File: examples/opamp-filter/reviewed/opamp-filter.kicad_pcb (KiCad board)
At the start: 2 copper layers, 58 x 42 mm, 22 parts, among them J1 IN, J2 5V, J3 OUT, U1 MCP6001R, U2 MCP6001R

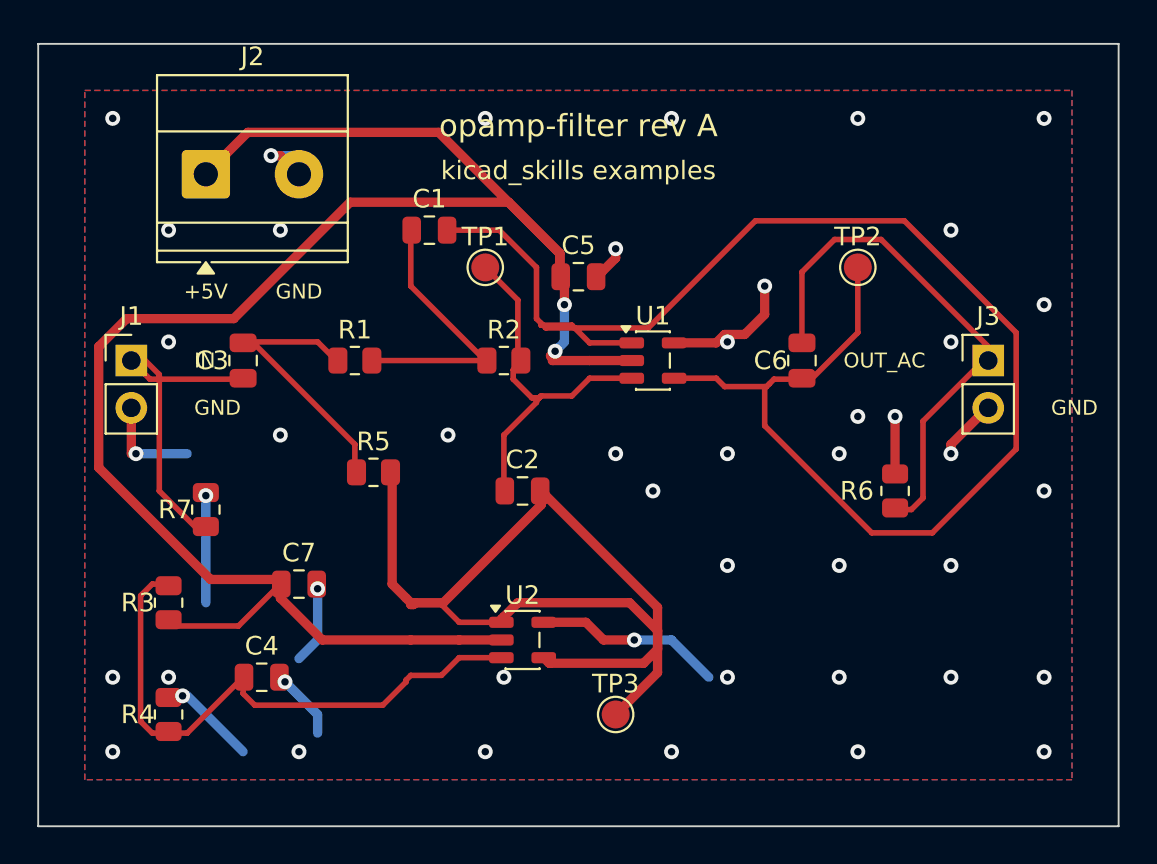
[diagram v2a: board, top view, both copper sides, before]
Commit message: Rip up copper that tours, and put a footprint's zones where the footprint is
The plots showed three things on the artwork side that no rule reported.

**A track that goes round the board to cover thirteen millimetres.** The
op-amp's feedback wrap had to get from one side of a SOT-23-5 to the other
and, routed last, took fifty-six millimetres of tour because everything
nearer was already spoken for. That is an ordering problem, so the loop that
fixes ordering fixes it: `_route_all` now reports what each track cost
against `route.wander`'s own baseline - imported, not copied, so the two
cannot drift - and the worst tour goes to the front and the set is routed
again. A track that still tours from first pick has nowhere better to be and
is left alone. The default order is shortest-first for the same reason: a
thirteen millimetre connection has few ways to be made and a forty
millimetre one has many. The learned order is now written on every change,
not only on success, because an afternoon of rip-ups is worth keeping when
the machine goes away in the middle.

**A keep-out sitting at the origin.** A footprint may carry zones of its own
and KiCad stores *those* in board coordinates while everything else in a
footprint is stored relative to it. The Pico module's two pad keep-outs had
been at (0, -6) for four rounds - off the board, keeping nothing out. DRC is
silent because an empty region violates no rule, and the only visible sign
was the plot: "fit to page" fits the bounding box, so every view of that
board came out at half scale in one corner with the rest blank.
`layout.zone_outside_outline` reports it; the placer moves it.

**Silkscreen printed through silkscreen.** The schematic has
`readability.text_over_text` and the board had nothing, though the board is
the harder case - a sheet can be zoomed and a bare board cannot.
`silk.text_over_text` measures it from the font size the file states; on
KiCad's demo boards it fires on 6 of 16, 173 times. The generator places t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
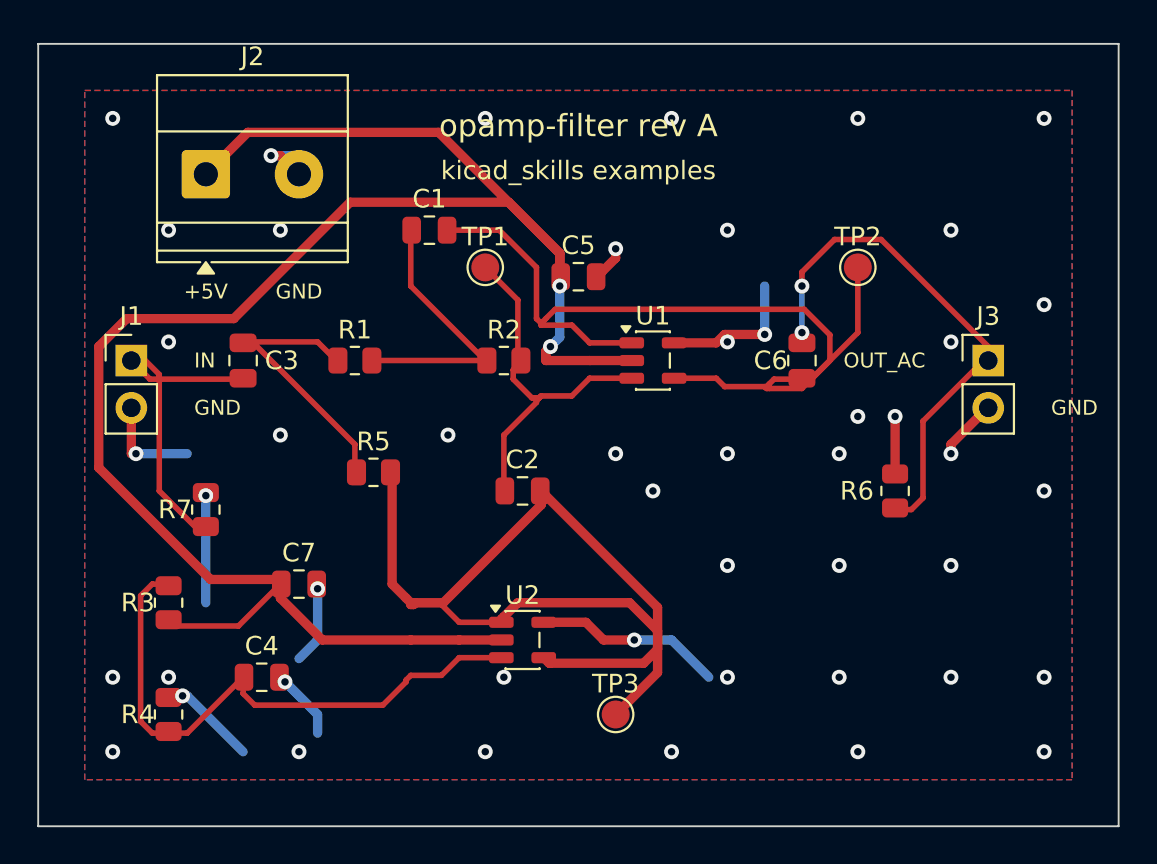
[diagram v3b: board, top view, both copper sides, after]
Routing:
- net /OUT: track 85.4 -> 50.9 mm
- net GND: track 53.8 -> 54.5 mm, vias 47 -> 48
- net /OUT_AC: vias 0 -> 2
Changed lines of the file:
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@@
     (tags "capacitor")
     (property "Reference" "C3"
-      (at 0.0 -1.68 0)
+      (at 0.0 2.075 0)
       (layer "F.SilkS")
       (effects
@@
     )
     (property "Voltage" "25V"
-      (at 0.0 -1.68 0)
+      (at 0.0 2.075 0)
       (layer "F.Fab")
       (hide yes)
@@
     )
     (property "Tolerance" "10%"
-      (at 0.0 -1.68 0)
+      (at 0.0 2.075 0)
       (layer "F.Fab")
       (hide yes)
@@
     )
     (property "MPN" "CL21B105KBFNNNE"
-      (at 0.0 -1.68 0)
+      (at 0.0 2.075 0)
       (layer "F.Fab")
       (hide yes)
@@
     )
     (property "Manufacturer" "Samsung"
-      (at 0.0 -1.68 0)
+      (at 0.0 2.075 0)
       (layer "F.Fab")
       (hide yes)
@@
     )
     (property "Datasheet" "https://product.samsungsem.com/mlcc/CL21B105KBFNNNE.do"
-      (at 0.0 -1.68 0)
+      (at 0.0 2.075 0)
       (layer "F.Fab")
       (hide yes)
@@
 	(segment (start 128.65 75.1) (end 127.0 75.1) (width 0.3) (layer "F.Cu") (net 7))
 	(segment (start 131.8625 77.0) (end 129.6 77.0) (width 0.5) (layer "F.Cu") (net 2))
-	(segment (start 129.6 77.0) (end 127.604 77.0) (width 0.5) (layer "F.Cu") (net 2))
-	(segment (start 127.604 77.0) (end 127.604 76.854) (width 0.5) (layer "F.Cu") (net 2))
-	(segment (start 127.604 76.854) (end 127.5 76.75) (width 0.5) (layer "F.Cu") (net 2))
-	(segment (start 127.5 76.75) (end 127.75 76.5) (width 0.5) (layer "F.Cu") (net 2))
+	(segment (start 129.6 77.0) (end 127.25 77.0) (width 0.5) (layer "F.Cu") (net 2))
+	(segment (start 127.25 77.0) (end 127.25 76.75) (width 0.5) (layer "F.Cu") (net 2))
+	(segment (start 127.25 76.75) (end 127.25 76.5) (width 0.5) (layer "F.Cu") (net 2))
+	(segment (start 127.25 76.5) (end 127.5 76.25) (width 0.5) (layer "F.Cu") (net 2))
 	(segment (start 131.8625 77.95) (end 129.6 77.95) (width 0.3) (layer "F.Cu") (net 3))
 	(segment (start 129.6 77.95) (end 128.65 78.9) (width 0.3) (layer "F.Cu") (net 3))
@@
 	(segment (start 134.1375 76.05) (end 136.4 76.05) (width 0.5) (layer "F.Cu") (net 1))
 	(segment (start 136.4 76.05) (end 136.85 75.6) (width 0.5) (layer "F.Cu") (net 1))
-	(segment (start 136.85 75.6) (end 137.925 75.6) (width 0.5) (layer "F.Cu") (net 1))
-	(segment (start 137.925 75.6) (end 139.0 74.525) (width 0.5) (layer "F.Cu") (net 1))
-	(segment (start 139.0 74.525) (end 139.0 73.0) (width 0.5) (layer "F.Cu") (net 1))
+	(segment (start 136.85 75.6) (end 139.0 75.6) (width 0.5) (layer "F.Cu") (net 1))
 	(segment (start 134.1375 77.95) (end 136.4 77.95) (width 0.3) (layer "F.Cu") (net 7))
 	(segment (start 136.4 77.95) (end 136.85 78.4) (width 0.3) (layer "F.Cu") (net 7))
@@
 	(segment (start 126.75 79.25) (end 126.75 79.15) (width 0.3) (layer "F.Cu") (net 3))
 	(segment (start 126.75 79.15) (end 127.0 78.9) (width 0.3) (layer "F.Cu") (net 3))
-	(segment (start 127.0 75.1) (end 127.1 75.1) (width 0.3) (layer "F.Cu") (net 7))
-	(segment (start 127.1 75.1) (end 127.25 75.25) (width 0.3) (layer "F.Cu") (net 7))
-	(segment (start 127.25 75.25) (end 132.75 75.25) (width 0.3) (layer "F.Cu") (net 7))
-	(segment (start 132.75 75.25) (end 138.5 69.5) (width 0.3) (layer "F.Cu") (net 7))
-	(segment (start 138.5 69.5) (end 146.5 69.5) (width 0.3) (layer "F.Cu") (net 7))
-	(segment (start 146.5 69.5) (end 152.5 75.5) (width 0.3) (layer "F.Cu") (net 7))
-	(segment (start 152.5 75.5) (end 152.5 81.75) (width 0.3) (layer "F.Cu") (net 7))
-	(segment (start 152.5 81.75) (end 148.0 86.25) (width 0.3) (layer "F.Cu") (net 7))
-	(segment (start 148.0 86.25) (end 144.75 86.25) (width 0.3) (layer "F.Cu") (net 7))
-	(segment (start 144.75 86.25) (end 139.0 80.5) (width 0.3) (layer "F.Cu") (net 7))
-	(segment (start 139.0 80.5) (end 139.0 78.4) (width 0.3) (layer "F.Cu") (net 7))
+	(segment (start 127.0 75.1) (end 127.0 75.0) (width 0.3) (layer "F.Cu") (net 7))
+	(segment (start 127.0 75.0) (end 127.25 74.75) (width 0.3) (layer "F.Cu") (net 7))
+	(segment (start 127.25 74.75) (end 127.75 74.25) (width 0.3) (layer "F.Cu") (net 7))
+	(segment (start 127.75 74.25) (end 141.125 74.25) (width 0.3) (layer "F.Cu") (net 7))
+	(segment (start 141.125 74.25) (end 142.5 75.625) (width 0.3) (layer "F.Cu") (net 7))
+	(segment (start 142.5 75.625) (end 142.5 77.0) (width 0.3) (layer "F.Cu") (net 7))
+	(segment (start 142.5 77.0) (end 141.0 78.5) (width 0.3) (layer "F.Cu") (net 7))
+	(segment (start 141.0 78.5) (end 139.25 78.5) (width 0.3) (layer "F.Cu") (net 7))
+	(segment (start 139.25 78.5) (end 139.1 78.5) (width 0.3) (layer "F.Cu") (net 7))
+	(segment (start 139.1 78.5) (end 139.0 78.4) (width 0.3) (layer "F.Cu") (net 7))
 	(segment (start 127.0 75.1) (end 127.0 75.0) (width 0.3) (layer "F.Cu") (net 7))
 	(segment (start 127.0 75.0) (end 126.75 74.75) (width 0.3) (layer "F.Cu") (net 7))
@@
 	(segment (start 126.75 72.0) (end 124.75 70.0) (width 0.3) (layer "F.Cu") (net 7))
 	(segment (start 124.75 70.0) (end 121.95 70.0) (width 0.3) (layer "F.Cu") (net 7))
-	(segment (start 141.0 76.05) (end 141.0 72.25) (width 0.3) (layer "F.Cu") (net 8))
+	(segment (start 141.0 76.05) (end 141.0 75.5) (width 0.3) (layer "F.Cu") (net 8))
+	(segment (start 141.0 75.5) (end 141.0 73.0) (width 0.3) (layer "B.Cu") (net 8))
+	(segment (start 141.0 73.0) (end 141.0 72.25) (width 0.3) (layer "F.Cu") (net 8))
 	(segment (start 141.0 72.25) (end 142.75 70.5) (width 0.3) (layer "F.Cu") (net 8))
 	(segment (start 142.75 70.5) (end 145.25 70.5) (width 0.3) (layer "F.Cu") (net 8))
@@
 	(segment (start 128.0 72.25) (end 128.0 72.45) (width 0.5) (layer "F.Cu") (net 2))
 	(segment (start 128.0 72.45) (end 128.05 72.5) (width 0.5) (layer "F.Cu") (net 2))
-	(segment (start 128.05 72.5) (end 128.05 72.55) (width 0.5) (layer "F.Cu") (net 2))
-	(segment (start 128.05 72.55) (end 128.25 72.75) (width 0.5) (layer "F.Cu") (net 2))
-	(segment (start 128.25 72.75) (end 128.25 74.0) (width 0.5) (layer "F.Cu") (net 2))
-	(segment (start 128.25 74.0) (end 128.25 76.0) (width 0.5) (layer "B.Cu") (net 2))
-	(segment (start 128.25 76.0) (end 127.75 76.5) (width 0.5) (layer "B.Cu") (net 2))
+	(segment (start 128.05 72.5) (end 128.05 72.7) (width 0.5) (layer "F.Cu") (net 2))
+	(segment (start 128.05 72.7) (end 128.0 72.75) (width 0.5) (layer "F.Cu") (net 2))
+	(segment (start 128.0 72.75) (end 128.0 73.0) (width 0.5) (layer "F.Cu") (net 2))
+	(segment (start 128.0 73.0) (end 128.0 75.75) (width 0.5) (layer "B.Cu") (net 2))
+	(segment (start 128.0 75.75) (end 127.5 76.25) (width 0.5) (layer "B.Cu") (net 2))
 	(segment (start 128.05 72.5) (end 128.05 72.3) (width 0.5) (layer "F.Cu") (net 2))
 	(segment (start 128.05 72.3) (end 128.0 72.25) (width 0.5) (layer "F.Cu") (net 2))
@@
 	(segment (start 107.75 95.0) (end 108.0 95.0) (width 0.5) (layer "B.Cu") (net 1))
 	(segment (start 108.0 95.0) (end 111.0 98.0) (width 0.5) (layer "B.Cu") (net 1))
+	(segment (start 139.0 75.6) (end 139.0 73.0) (width 0.5) (layer "B.Cu") (net 1))
 	(segment (start 132.0 92.0) (end 134.0 92.0) (width 0.5) (layer "B.Cu") (net 1))
 	(segment (start 134.0 92.0) (end 136.0 94.0) (width 0.5) (layer "B.Cu") (net 1))
@@
 	(via (at 133.0 84.0) (size 0.8) (drill 0.4) (layers "F.Cu" "B.Cu") (net 1))
 	(via (at 144.0 80.0) (size 0.8) (drill 0.4) (layers "F.Cu" "B.Cu") (net 1))
-	(via (at 128.25 74.0) (size 0.8) (drill 0.4) (layers "F.Cu" "B.Cu") (net 2))
-	(via (at 127.75 76.5) (size 0.8) (drill 0.4) (layers "F.Cu" "B.Cu") (net 2))
+	(via (at 141.0 75.5) (size 0.8) (drill 0.4) (layers "F.Cu" "B.Cu") (net 8))
+	(via (at 141.0 73.0) (size 0.8) (drill 0.4) (layers "F.Cu" "B.Cu") (net 8))
+	(via (at 128.0 73.0) (size 0.8) (drill 0.4) (layers "F.Cu" "B.Cu") (net 2))
+	(via (at 127.5 76.25) (size 0.8) (drill 0.4) (layers "F.Cu" "B.Cu") (net 2))
 	(via (at 105.25 82.0) (size 0.8) (drill 0.4) (layers "F.Cu" "B.Cu") (net 1))
 	(via (at 149.0 82.0) (size 0.8) (drill 0.4) (layers "F.Cu" "B.Cu") (net 1))
@@
 	(via (at 132.0 92.0) (size 0.8) (drill 0.4) (layers "F.Cu" "B.Cu") (net 1))
 	(via (at 131.0 71.0) (size 0.8) (drill 0.4) (layers "F.Cu" "B.Cu") (net 1))
-	(via (at 139.0 73.0) (size 0.8) (drill 0.4) (layers "F.Cu" "B.Cu") (net 1))
+	(via (at 139.0 75.6) (size 0.8) (drill 0.4) (layers "F.Cu" "B.Cu") (net 1))
 	(via (at 104.0 64.0) (size 0.8) (drill 0.4) (layers "F.Cu" "B.Cu") (net 1))
 	(via (at 104.0 98.0) (size 0.8) (drill 0.4) (layers "F.Cu" "B.Cu") (net 1))
@@
 	(via (at 107.0 70.0) (size 0.8) (drill 0.4) (layers "F.Cu" "B.Cu") (net 1))
 	(via (at 113.0 70.0) (size 0.8) (drill 0.4) (layers "F.Cu" "B.Cu") (net 1))
+	(via (at 137.0 70.0) (size 0.8) (drill 0.4) (layers "F.Cu" "B.Cu") (net 1))
 	(via (at 149.0 70.0) (size 0.8) (drill 0.4) (layers "F.Cu" "B.Cu") (net 1))
 	(via (at 107.0 76.0) (size 0.8) (drill 0.4) (layers "F.Cu" "B.Cu") (net 1))

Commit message: Learn the drawing from the boards people drew
The brief for this round: relying on the autorouter and the numbers alone is
not enough - organise what pictorial correctness looks like from ordinary
circuits and open designs, and improve the drawing itself. So it starts in
KiCad's own demo corpus, measured and looked at, and ends with the habits
pushed into the generator.

tools/board_signature.py (new) reduces "looks autorouted" to five numbers.
Hand-routed two-layer boards cluster tightly: 10-47% of copper on the second
face, median segments 1.8-3.5 mm, 9-25 corners per decimetre, 91-98% of them
45s, 0.3-16 vias per decimetre. Rendering interf_u beside our boards says the
same thing in one glance: a layer has a direction, a bus travels as a bundle,
a person covers an offset with the long straight and one diagonal.

Three habits, now in the generator:

* Router.route(follow=...): cells beside a sibling net's path are discounted,
  so a bus (nets sharing a name prefix - I2S_*, SPI_*) travels as parallel
  lanes in one corridor. The discount is a fraction of a step, so it never
  buys a detour.
* _doglegged: every wiggly stretch is redrawn as the human stroke - the
  straight along the dominant direction plus one 45 - when the dogleg is
  clear, recursing into halves where a crossing blocks the whole. The op-amp
  board's median segment rose from 0.75 mm and its corner rate fell from
  38/dm; the FPGA board landed at 1.54 mm and 17.8/dm, inside the human band.
* Purposeful stitching: the 6 mm via carpet is gone. A ring at the rim, vias
  beside every back-layer crossing (where the plane is actually cut), and a
  coarse 12 mm mesh so no pour orphans. Vias/dm: buck 41 -> 18, carrier
  28 -> 13, all five inside the corpus band, pour_fragmented still silent.

Three failures the round produced and what they taught:

* pinned(): reshaping may not move copper off any point inside an own-net
  pad - the centre alone was not enough, a routed run touches off-centre and
  the ove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
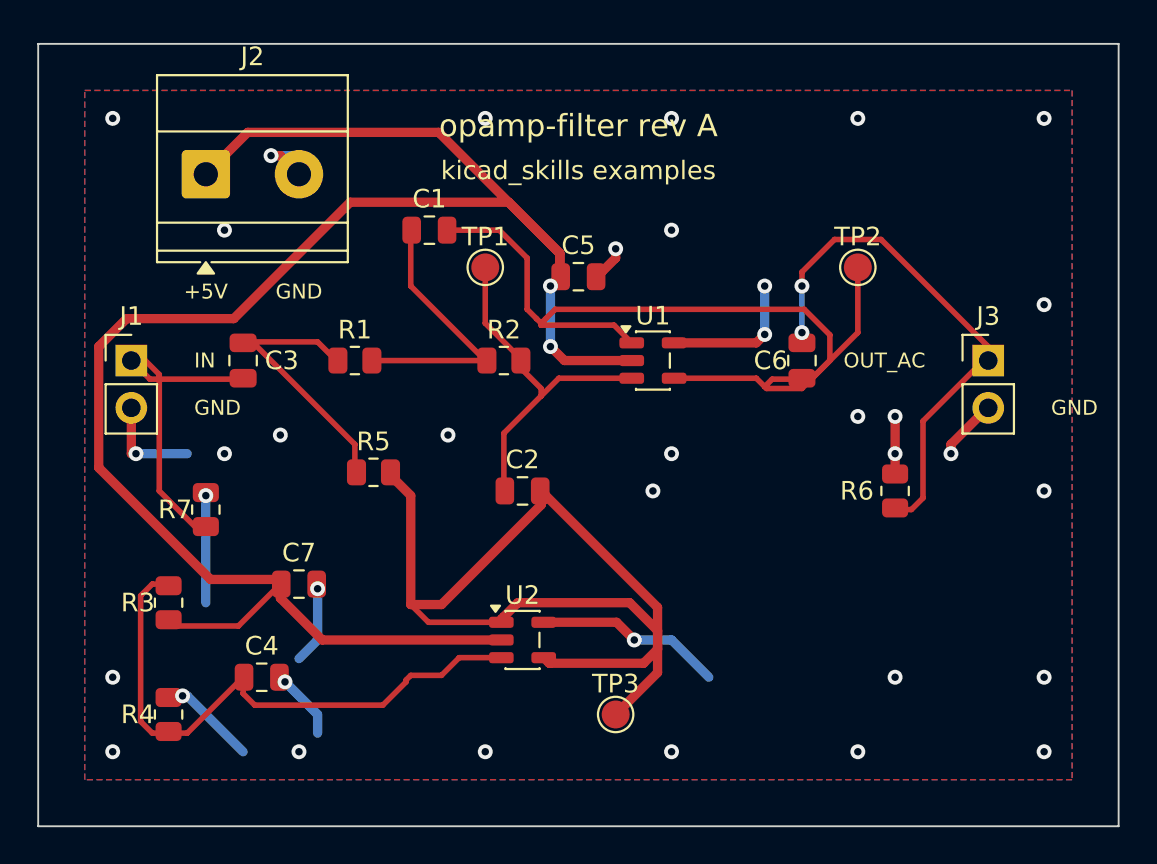
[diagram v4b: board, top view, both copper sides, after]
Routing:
- net +5V: track 103.3 -> 102.6 mm
- net /FILT_IN: track 20.1 -> 19.5 mm
- net GND: vias 48 -> 37
